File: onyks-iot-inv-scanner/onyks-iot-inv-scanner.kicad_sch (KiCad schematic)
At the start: 13 parts, among them SW1 EN, SW2 BOOT, U1 ESP32-WROOM-32D

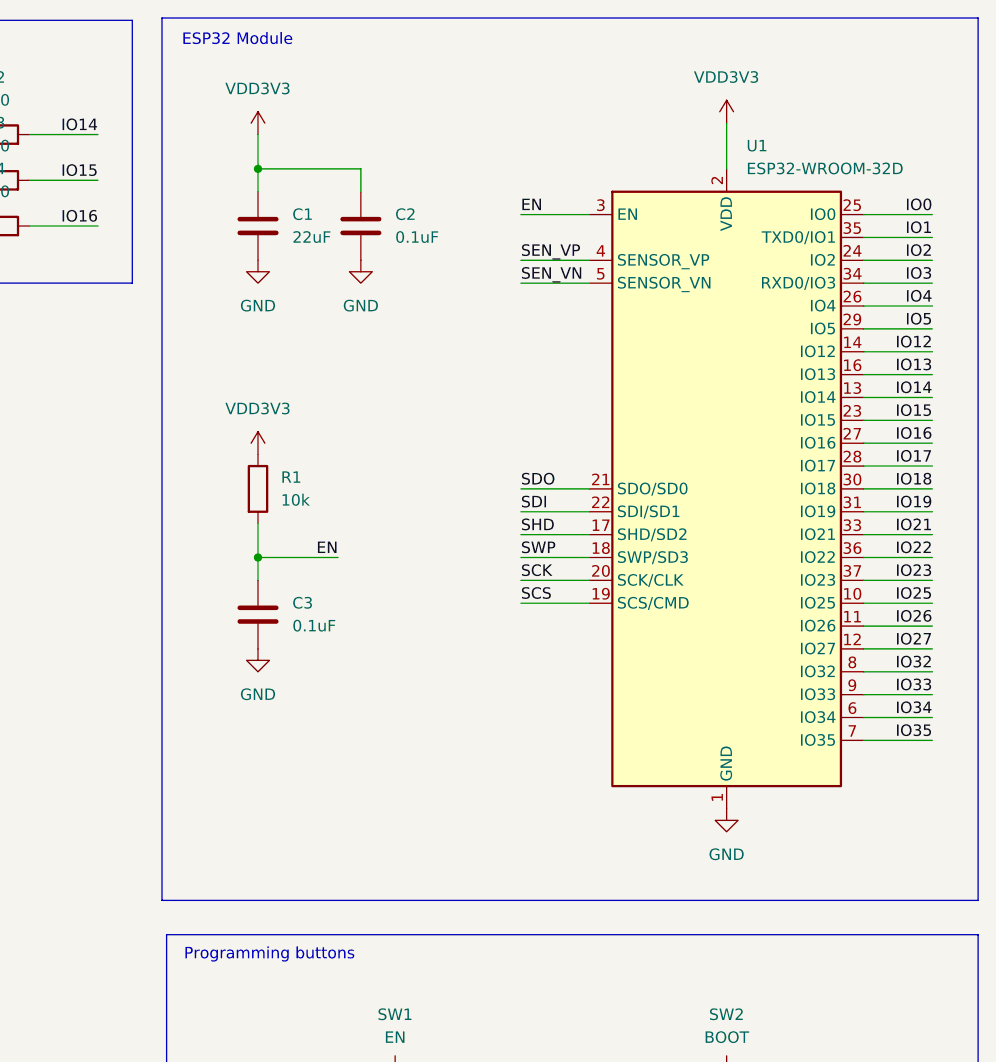
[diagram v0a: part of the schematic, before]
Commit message: changed controller and updated component list
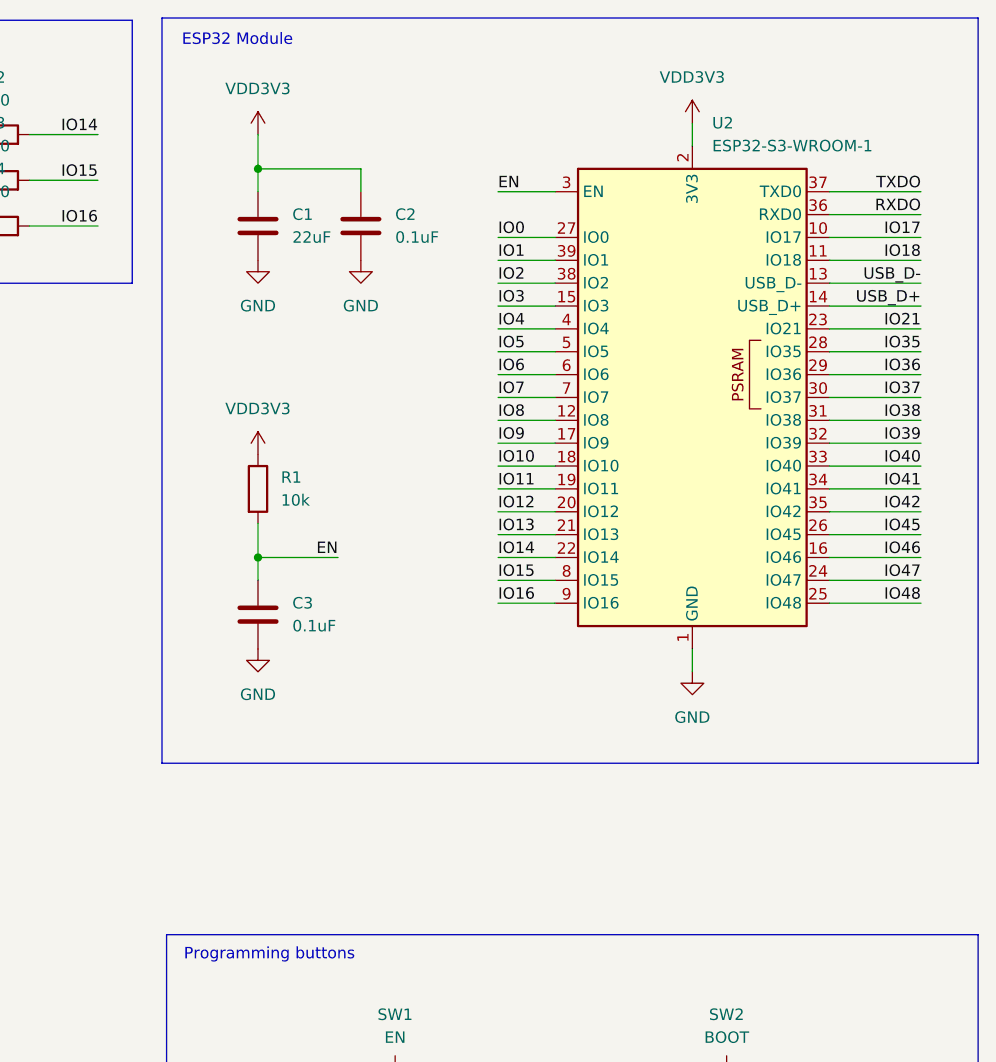
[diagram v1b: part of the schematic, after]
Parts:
- removed U1: ESP32-WROOM-32D, RF_Module:ESP32-WROOM-32D, symbol RF_Module:ESP32-WROOM-32D
- added U2: ESP32-S3-WROOM-1, RF_Module:ESP32-S3-WROOM-1, symbol RF_Module:ESP32-S3-WROOM-1
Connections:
- net EN: now also U2.3 (EN)
- net GND: now also U2.1 (GND), U2.40 (GND), U2.41 (GND)
- net IO0: now also U2.27 (IO0)
- net IO1: now also U2.39 (IO1)
- net IO12: now also U2.20 (IO12)
- net IO13: now also U2.21 (IO13)
- net IO14: now also U2.22 (IO14)
- net IO15: now also U2.8 (IO15)
- net IO16: now also U2.9 (IO16)
- net IO17: now also U2.10 (IO17)
- net IO18: now also U2.11 (IO18)
- net IO2: now also U2.38 (IO2)
- net IO21: now also U2.23 (IO21)
- net IO3: now also U2.15 (IO3)
- net IO35: now also U2.28 (IO35)
- net IO4: now also U2.4 (IO4)
- net IO5: now also U2.5 (IO5)
- net VDD3V3: now also U2.2 (3V3)
- new net IO10: U2.18 (IO10)
- new net IO11: U2.19 (IO11)
- new net IO36: U2.29 (IO36)
- new net IO37: U2.30 (IO37)
- new net IO38: U2.31 (IO38)
- new net IO39: U2.32 (IO39)
- new net IO40: U2.33 (IO40)
- new net IO41: U2.34 (IO41)
- new net IO42: U2.35 (IO42)
- new net IO45: U2.26 (IO45)
- new net IO46: U2.16 (IO46)
- new net IO47: U2.24 (IO47)
- new net IO48: U2.25 (IO48)
- new net IO6: U2.6 (IO6)
- new net IO7: U2.7 (IO7)
- new net IO8: U2.12 (IO8)
- new net IO9: U2.17 (IO9)
- new net RXDO: U2.36 (RXD0)
- new net TXDO: U2.37 (TXD0)
- new net USB_D+: U2.14 (USB_D+)
- new net USB_D-: U2.13 (USB_D-)

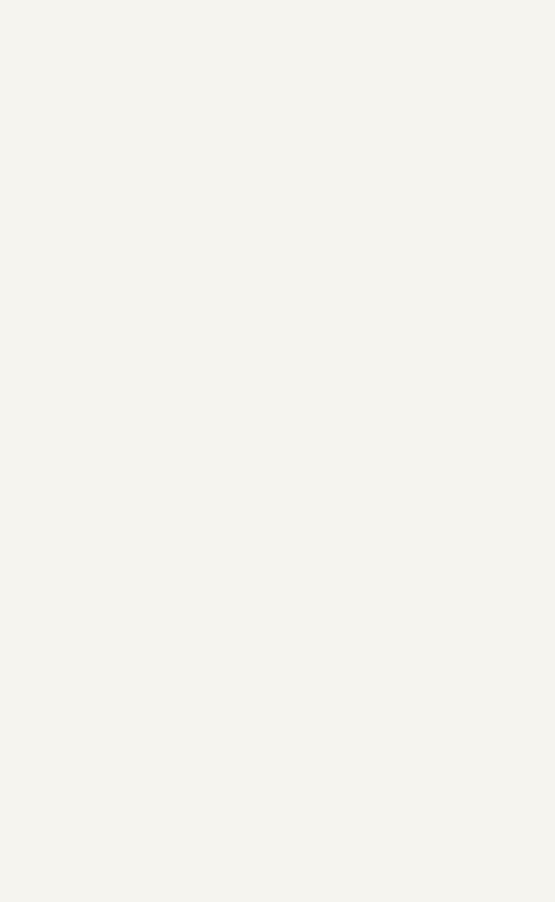
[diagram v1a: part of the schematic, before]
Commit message: deleted unnecessary files
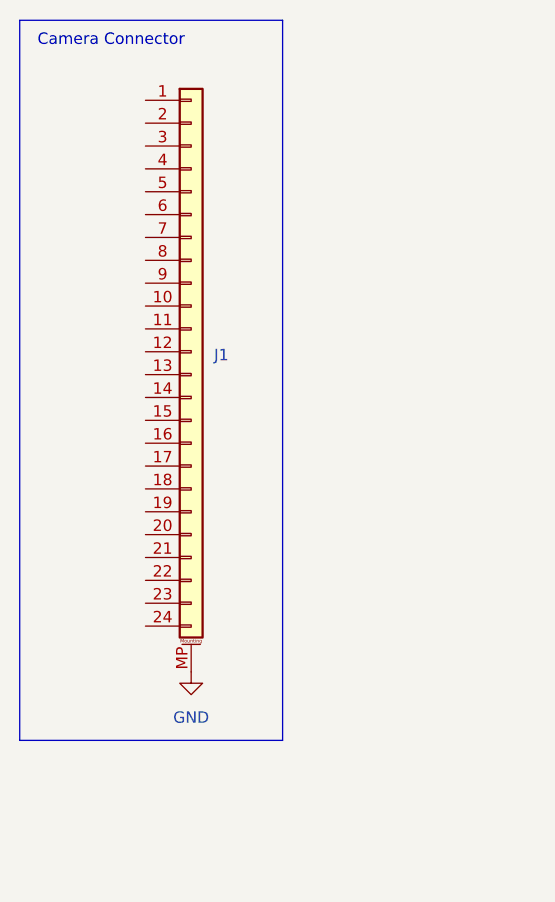
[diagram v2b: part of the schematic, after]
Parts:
- added J1: Conn_01x24_MountingPin, Connector_FFC-FPC:Molex_502244-2430_1x24-1MP_P0.5mm_Horizontal, symbol Connector_Generic_MountingPin:Conn_01x24_MountingPin
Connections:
- net GND: now also J1.MP (MountPin)
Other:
- note added: "Camera Connector"
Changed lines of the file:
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@@
+	)
+	(rectangle
+		(start 15.24 15.24)
+		(end 44.45 95.25)
+		(stroke
+			(width 0)
+			(type default)
+		)
+		(fill
+			(type none)
+		)
 	)
 	(rectangle
@@
 		)
 	)
+	(text "Camera Connector"
+		(exclude_from_sim no)
+		(at 25.4 17.526 0)
+		(effects
+			(font
+				(size 1.27 1.27)
+			)
+		)
+	)
 	(text "ESP32 Module"
 		(exclude_from_sim no)
@@
 	)
 	(symbol
+		(lib_id "Connector_Generic_MountingPin:Conn_01x24_MountingPin")
+		(at 34.29 52.07 0)
+		(unit 1)
+		(exclude_from_sim no)
+		(in_bom yes)
+		(on_board yes)
+		(dnp no)
+		(fields_autoplaced yes)
+		(property "Reference" "J1"
+			(at 36.83 52.4255 0)
+			(effects
+				(font
+					(size 1.27 1.27)
+				)
+				(justify left)
+			)
+		)
+		(property "Value" "Conn_01x24_MountingPin"
+			(at 36.83 54.9655 0)
+			(effects
+				(font
+					(size 1.27 1.27)
+				)
+				(justify left)
+				(hide yes)
+			)
+		)
+		(property "Footprint" "Connector_FFC-FPC:Molex_502244-2430_1x24-1MP_P0.5mm_Horizontal"
+			(at 34.29 52.07 0)
+			(effects
+				(font
+					(size 1.27 1.27)
+				)
+				(hide yes)
+			)
+		)
+		(property "Datasheet" "~"
+			(at 34.29 52.07 0)
+			(effects
+				(font
+					(size 1.27 1.27)
+				)
+				(hide yes)
+			)
+		)
+		(property "Description" "Generic connectable mounting pin connector, single row, 01x24, script generated (kicad-library-utils/schlib/autogen/connector/)"
+			(at 34.29 52.07 0)
+			(effects
+				(font
+					(size 1.27 1.27)
+				)
+				(hide yes)
+			)
+		)
+		(pin "19"
+		)
+		(pin "2"
+		)
+		(pin "18"
+		)
+		(pin "9"
+		)
+		(pin "MP"
+		)
+		(pin "23"
+		)
+		(pin "4"
+		)
+		(pin "3"
+		)
+		(pin "8"
+		)
+		(pin "15"
+		)
+		(pin "16"
+		)
+		(pin "7"
+		)
+		(pin "22"
+		)
+		(pin "17"
+		)
+		(pin "6"
+		)
+		(pin "13"
+		)
+		(pin "21"
+		)
+		(pin "14"
+		)
+		(pin "12"
+		)
+		(pin "11"
+		)
+		(pin "10"
+		)
+		(pin "20"
+		)
+		(pin "24"
+		)
+		(pin "5"
+		)
+		(pin "1"
+		)
+		(instances
+			(project ""
+				(path "/37956750-1b3c-4b3f-94c5-40fd1631cd50"
+					(reference "J1")
+					(unit 1)
+				)
+			)
+		)
+	)
+	(symbol
 		(lib_id "Device:C")
 		(at 217.17 143.51 90)
@@
 					(unit 1)
 				)
+			)
+		)
+	)
+	(symbol
+		(lib_id "power:GND")
+		(at 34.29 87.63 0)
+		(unit 1)
+		(exclude_from_sim no)
+		(in_bom yes)
+		(on_board yes)
+		(dnp no)
+		(fields_autoplaced yes)
+		(property "Reference" "#PWR011"
+			(at 34.29 93.98 0)
+			(effects
+				(font
+					(size 1.27 1.27)
+				)
+				(hide yes)
+			)
+		)
+		(property "Value" "GND"
+			(at 34.29 92.71 0)
+			(effects
+				(font
+					(size 1.27 1.27)
+				)
+			)
+		)
+		(property "Footprint" ""
+			(at 34.29 87.63 0)
+			(effects
+				(font
+					(size 1.27 1.27)
+				)
+				(hide yes)
+			)
+		)
+		(property "Datasheet" ""
+			(at 34.29 87.63 0)
+			(effects
+				(font
+					(size 1.27 1.27)
+				)
+				(hide yes)
+			)
+		)
+		(property "Description" "Power symbol creates a global label with name \"GND\" , ground"
+			(at 34.29 87.63 0)
+			(effects
+				(font
+					(size 1.27 1.27)
+				)
+				(hide yes)
+			)
+		)
+		(pin "1"
+		)
+		(instances
+			(project ""
+				(path "/37956750-1b3c-4b3f-94c5-40fd1631cd50"
+					(reference "#PWR011")
+					(unit 1)
+				)
